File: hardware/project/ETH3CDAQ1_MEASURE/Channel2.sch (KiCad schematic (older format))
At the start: 49 parts, among them U1401 LT1355, U1402 DG211, U1403 DG419LDY, U1404 DG419LDY, U1405 OPA192, U1406 74LVC1GU04DRL, U1407 ADS8681RUM, U1408 74HCT595

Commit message: PCB design
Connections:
- net +5VF is gone; now on net +5V: U1407.16 (AVDD)
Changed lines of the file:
@@
 Wire Wire Line
 	4550 10550 4800 10550
-$Comp
-L ETH3CDAQ1:+5VF #PWR?
-U 1 1 5FFA8BC2
-P 12200 4050
-AR Path="/5FB85416/5FFA8BC2" Ref="#PWR?"  Part="1"
-AR Path="/5FF801EB/5FFA8BC2" Ref="#PWR01438"  Part="1"
-F 0 "#PWR01438" H 12200 3900 50  0001 C CNN
-F 1 "+5VF" H 12215 4223 50  0000 C CNN
-F 2 "" H 12200 4050 50  0001 C CNN
-F 3 "" H 12200 4050 50  0001 C CNN
-	1    12200 4050
-	1    0    0    -1
-$EndComp
 Wire Wire Line
 	11850 4600 11300 4600
@@
 Text HLabel 14150 6000 2    50   BiDi ~ 0
 SR1_QH
+$Comp
+L power:+5V #PWR0101
+U 1 1 5FD8421C
+P 12200 4050
+F 0 "#PWR0101" H 12200 3900 50  0001 C CNN
+F 1 "+5V" H 12215 4223 50  0000 C CNN
+F 2 "" H 12200 4050 50  0001 C CNN
+F 3 "" H 12200 4050 50  0001 C CNN
+	1    12200 4050
+	1    0    0    -1
+$EndComp
 $EndSCHEMATC

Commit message: PCB layout
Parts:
- added R906: 0, Resistor_SMD:R_0603_1608Metric_Pad0.98x0.95mm_HandSolder, symbol Device:R
- renumbered C1401 to C901, C1402 to C902, C1403 to C903, C1404 to C904, C1405 to C905, C1406 to C906, C1407 to C907, C1408 to C908, C1409 to C909, C1410 to C910, C1411 to C911, C1412 to C912, C1413 to C913, C1414 to C914, C1415 to C915, C1416 to C916, C1417 to C917, C1418 to C918, C1419 to C919, C1420 to C920, C1421 to C921, C1422 to C922, C1423 to C923, C1424 to C924, C1425 to C925, R1401 to R901, R1402 to R902, R1403 to R903, R1404 to R904, R1405 to R905, R1406 to R907, R1407 to R908, R1408 to R909, R1409 to R910, R1410 to R911, R1411 to R912, R1412 to R913, R1413 to R914, R1414 to R915, R1415 to R916, R1416 to R917, U1401 to U901, U1402 to U902, U1403 to U903, U1404 to U904, U1405 to U905, U1406 to U906, U1407 to U907, U1408 to U908
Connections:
- net at U902.10, U902.15, U902.3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: now also R906.2
- net at U903.1, U905.3 (+), U905.6: now also R906.1

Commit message: Fixed mistake with DG419. Never use DG419Lxx variant.
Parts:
- U903, U904: value DG419LDY -> DG419DY; symbol Analog_Switch:DG419LDY -> Analog_Switch:DG419xY
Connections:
- net at R906.2, U902.10, U902.15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: now also U905.3 (+); no longer U905.2 (-)
- net at R906.1, U903.1, U905.6: now also U905.2 (-); no longer U905.3 (+)
- no-connect marks 7 -> 9
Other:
- note added: "RN - CAY10-681J4LF"
- note removed: "RN - ACASA1001S1001P100"
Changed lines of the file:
@@
 $EndDescr
 Text Notes 3900 8250 0    50   ~ 0
-RN -  ACASA1001S1001P100
+RN -  CAY10-681J4LF
 $Comp
 L ETH3CDAQ1:DG211 U?
@@
 $EndComp
 $Comp
-L Analog_Switch:DG419LDY U?
+L Analog_Switch:DG419xY U?
 U 2 1 5FFA898C
 P 2450 10050
@@
 AR Path="/5FF801EB/5FFA898C" Ref="U903"  Part="2"
 F 0 "U903" H 2730 10096 50  0000 L CNN
-F 1 "DG419LDY" H 2730 10005 50  0000 L CNN
+F 1 "DG419DY" H 2730 10005 50  0000 L CNN
 F 2 "Package_SO:SOIC-8_3.9x4.9mm_P1.27mm" H 2450 9750 50  0001 C CNN
 F 3 "https://datasheets.maximintegrated.com/en/ds/DG417-DG419.pdf" H 2450 10050 50  0001 C CNN
@@
 $EndComp
 $Comp
-L Analog_Switch:DG419LDY U?
+L Analog_Switch:DG419xY U?
 U 2 1 5FFA8992
 P 3300 10050
@@
 AR Path="/5FF801EB/5FFA8992" Ref="U904"  Part="2"
 F 0 "U904" H 3580 10096 50  0000 L CNN
-F 1 "DG419LDY" H 3580 10005 50  0000 L CNN
+F 1 "DG419DY" H 3580 10005 50  0000 L CNN
 F 2 "Package_SO:SOIC-8_3.9x4.9mm_P1.27mm" H 3300 9750 50  0001 C CNN
 F 3 "https://datasheets.maximintegrated.com/en/ds/DG417-DG419.pdf" H 3300 10050 50  0001 C CNN
@@
 $EndComp
 $Comp
-L Analog_Switch:DG419LDY U?
+L Analog_Switch:DG419xY U?
 U 1 1 5FFA8A0A
 P 5700 4500
@@
 AR Path="/5FF801EB/5FFA8A0A" Ref="U903"  Part="1"
 F 0 "U903" H 5700 4742 50  0000 C CNN
-F 1 "DG419LDY" H 5700 4651 50  0000 C CNN
+F 1 "DG419DY" H 5700 4651 50  0000 C CNN
 F 2 "Package_SO:SOIC-8_3.9x4.9mm_P1.27mm" H 5700 4200 50  0001 C CNN
 F 3 "https://datasheets.maximintegrated.com/en/ds/DG417-DG419.pdf" H 5700 4500 50  0001 C CNN
@@
 $EndComp
 $Comp
-L Analog_Switch:DG419LDY U?
+L Analog_Switch:DG419xY U?
 U 1 1 5FFA8A10
 P 10050 4500
@@
 AR Path="/5FF801EB/5FFA8A10" Ref="U904"  Part="1"
 F 0 "U904" H 10050 4742 50  0000 C CNN
-F 1 "DG419LDY" H 10050 4651 50  0000 C CNN
+F 1 "DG419DY" H 10050 4651 50  0000 C CNN
 F 2 "Package_SO:SOIC-8_3.9x4.9mm_P1.27mm" H 10050 4200 50  0001 C CNN
 F 3 "https://datasheets.maximintegrated.com/en/ds/DG417-DG419.pdf" H 10050 4500 50  0001 C CNN
@@
 AR Path="/5FB85416/5FFA8C30" Ref="U?"  Part="1"
 AR Path="/5FF801EB/5FFA8C30" Ref="U905"  Part="1"
-F 0 "U905" H 4950 4850 50  0000 L CNN
-F 1 "OPA192" H 4900 4750 50  0000 L CNN
+F 0 "U905" H 4950 4350 50  0000 L CNN
+F 1 "OPA192" H 4900 4450 50  0000 L CNN
 F 2 "Package_SO:SOIC-8_3.9x4.9mm_P1.27mm" H 4900 4650 50  0001 C CNN
 F 3 "" H 4900 4750 50  0001 C CNN
 	1    4850 4600
-	1    0    0    -1
+	1    0    0    1
 $EndComp
 Wire Wire Line
@@
 L ETH3CDAQ1:+18V #PWR?
 U 1 1 5FFA8C3B
-P 4750 4300
+P 4750 4900
 AR Path="/5FB85416/5FFA8C3B" Ref="#PWR?"  Part="1"
 AR Path="/5FF801EB/5FFA8C3B" Ref="#PWR0918"  Part="1"
-F 0 "#PWR0918" H 4750 4150 50  0001 C CNN
-F 1 "+18V" H 4765 4473 50  0000 C CNN
-F 2 "" H 4750 4300 50  0001 C CNN
-F 3 "" H 4750 4300 50  0001 C CNN
-	1    4750 4300
-	1    0    0    -1
-$EndComp
-$Comp
-L ETH3CDAQ1:-18V #PWR?
-U 1 1 5FFA8C41
-P 4750 4900
-AR Path="/5FB85416/5FFA8C41" Ref="#PWR?"  Part="1"
-AR Path="/5FF801EB/5FFA8C41" Ref="#PWR0919"  Part="1"
-F 0 "#PWR0919" H 4750 4750 50  0001 C CNN
-F 1 "-18V" H 4765 5073 50  0000 C CNN
+F 0 "#PWR0918" H 4750 4750 50  0001 C CNN
+F 1 "+18V" H 4765 5073 50  0000 C CNN
 F 2 "" H 4750 4900 50  0001 C CNN
 F 3 "" H 4750 4900 50  0001 C CNN
 	1    4750 4900
 	-1   0    0    1
+$EndComp
+$Comp
+L ETH3CDAQ1:-18V #PWR?
+U 1 1 5FFA8C41
+P 4750 4300
+AR Path="/5FB85416/5FFA8C41" Ref="#PWR?"  Part="1"
+AR Path="/5FF801EB/5FFA8C41" Ref="#PWR0919"  Part="1"
+F 0 "#PWR0919" H 4750 4150 50  0001 C CNN
+F 1 "-18V" H 4765 4473 50  0000 C CNN
+F 2 "" H 4750 4300 50  0001 C CNN
+F 3 "" H 4750 4300 50  0001 C CNN
+	1    4750 4300
+	1    0    0    -1
 $EndComp
 Wire Wire Line
@@
 	5250 5400 5250 4600
 NoConn ~ 13350 4400
+NoConn ~ 4850 4300
+NoConn ~ 4850 4900
 $EndSCHEMATC

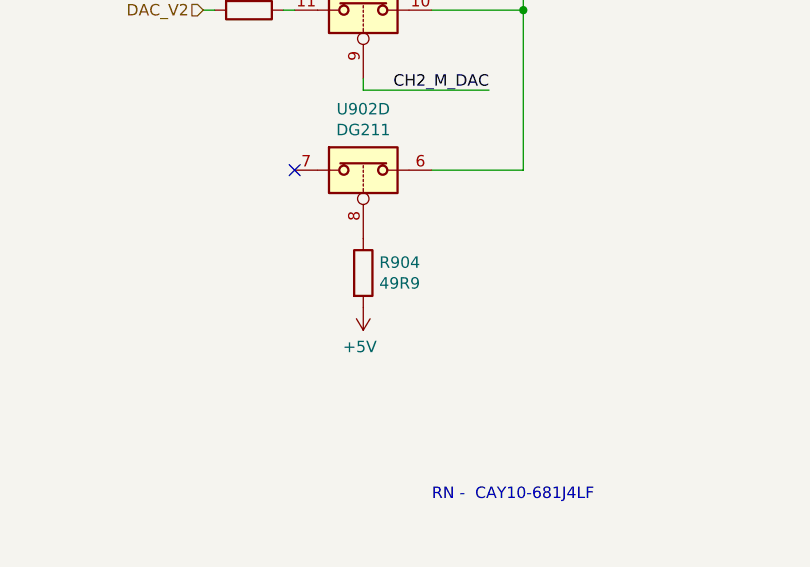
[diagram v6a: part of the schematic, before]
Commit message: STM32H7+FreeRTOS+LwIP works, thanks to this guide https://community.st.com/s/article/How-to-create-project-for-STM32H7-with-Ethernet-and-LwIP-stack-working. Add a 100ms delay before LWiP Init function.
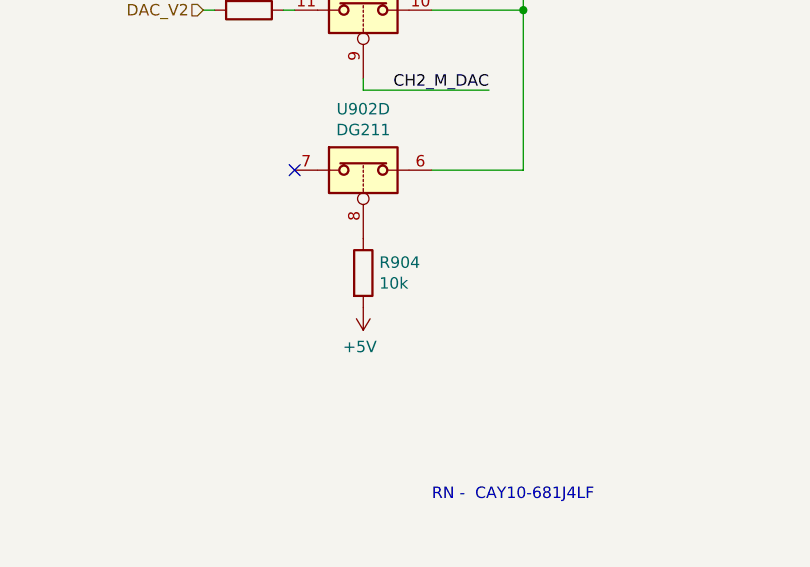
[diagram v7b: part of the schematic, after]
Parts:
- R904: value 49R9 -> 10k
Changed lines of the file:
@@
 AR Path="/5FF801EB/5FFA8B46" Ref="R904"  Part="1"
 F 0 "R904" H 3670 7296 50  0000 L CNN
-F 1 "49R9" H 3670 7205 50  0000 L CNN
+F 1 "10k" H 3670 7205 50  0000 L CNN
 F 2 "Resistor_SMD:R_0603_1608Metric_Pad0.98x0.95mm_HandSolder" V 3530 7250 50  0001 C CNN
 F 3 "~" H 3600 7250 50  0001 C CNN
